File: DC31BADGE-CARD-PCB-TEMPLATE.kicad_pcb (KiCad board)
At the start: 2 copper layers, 265.2 x 114.6 mm, 7 parts

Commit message: Adjusted scale
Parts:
- removed the G*** at (146.8, 102.9) (x7)
- added G*** (x7): LOGO, LOGO, F.Cu at (143.2, 89.0)
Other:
- board size 265.2 x 114.6 mm -> 40.9 x 92.8 mm

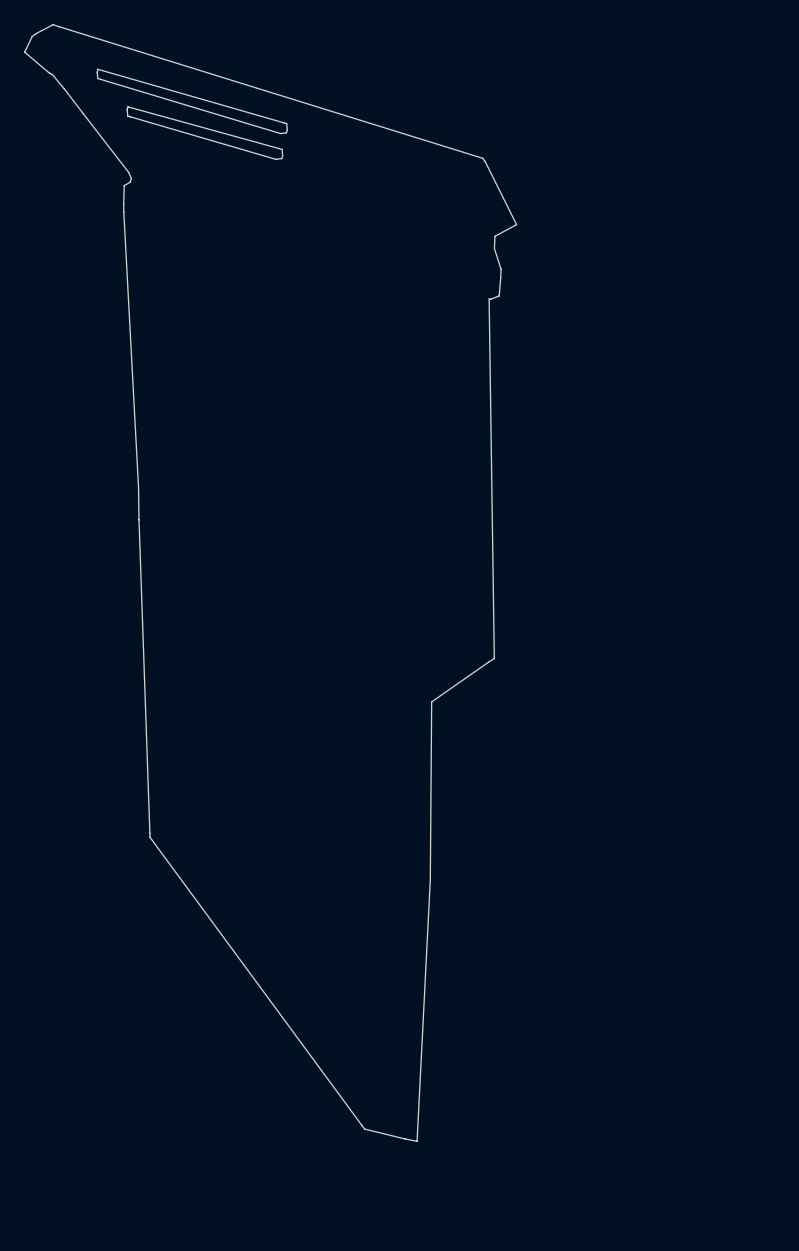
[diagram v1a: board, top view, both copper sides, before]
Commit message: Changed orientation and added edge cut nodes
Changed orientation to match what was provided originally, adjusted scaled to make width 30mm wide, added nodes to edgecut path in Inkscape to maintain edge details.
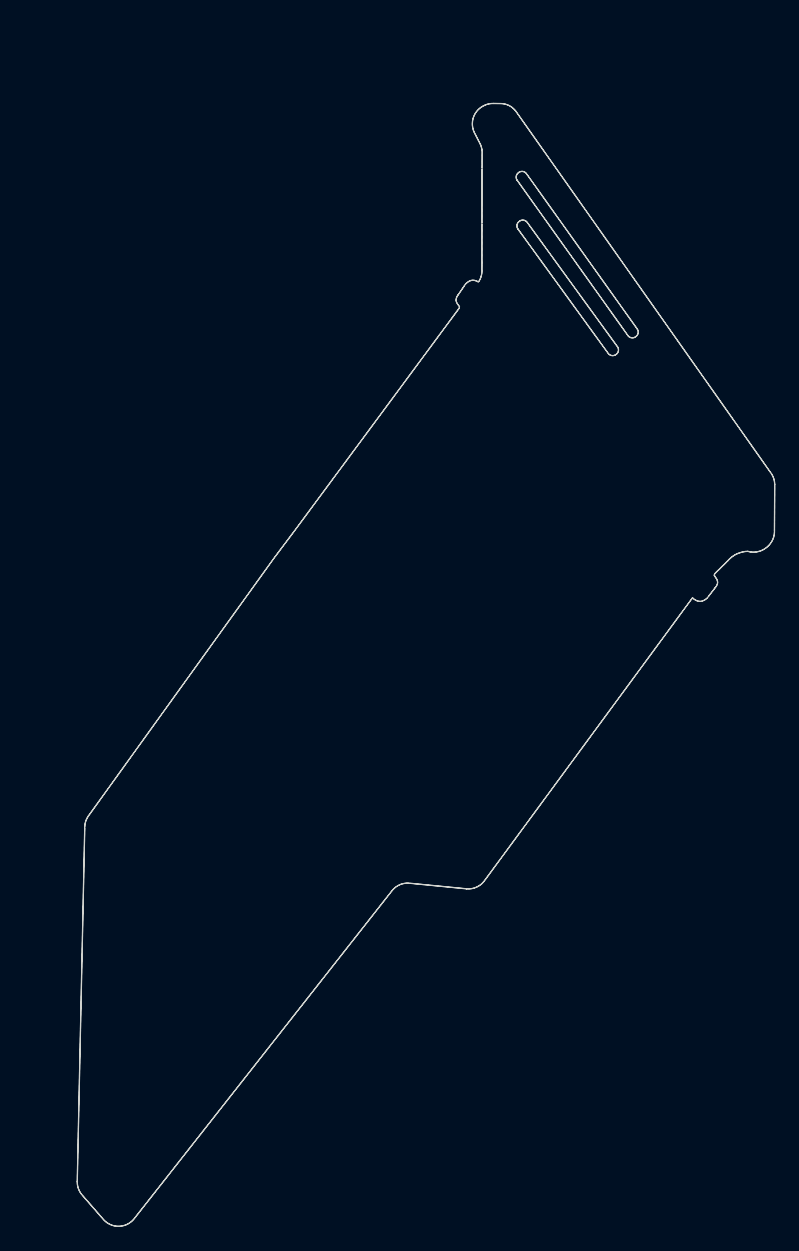
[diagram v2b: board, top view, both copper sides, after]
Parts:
- removed the G*** at (143.2, 89.0) (x7)
- added G*** (x7): LOGO, LOGO, F.Cu at (154.9, 96.5)
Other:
- board size 40.9 x 92.8 mm -> 57.9 x 93.3 mm
